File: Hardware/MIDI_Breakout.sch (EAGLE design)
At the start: 25 parts

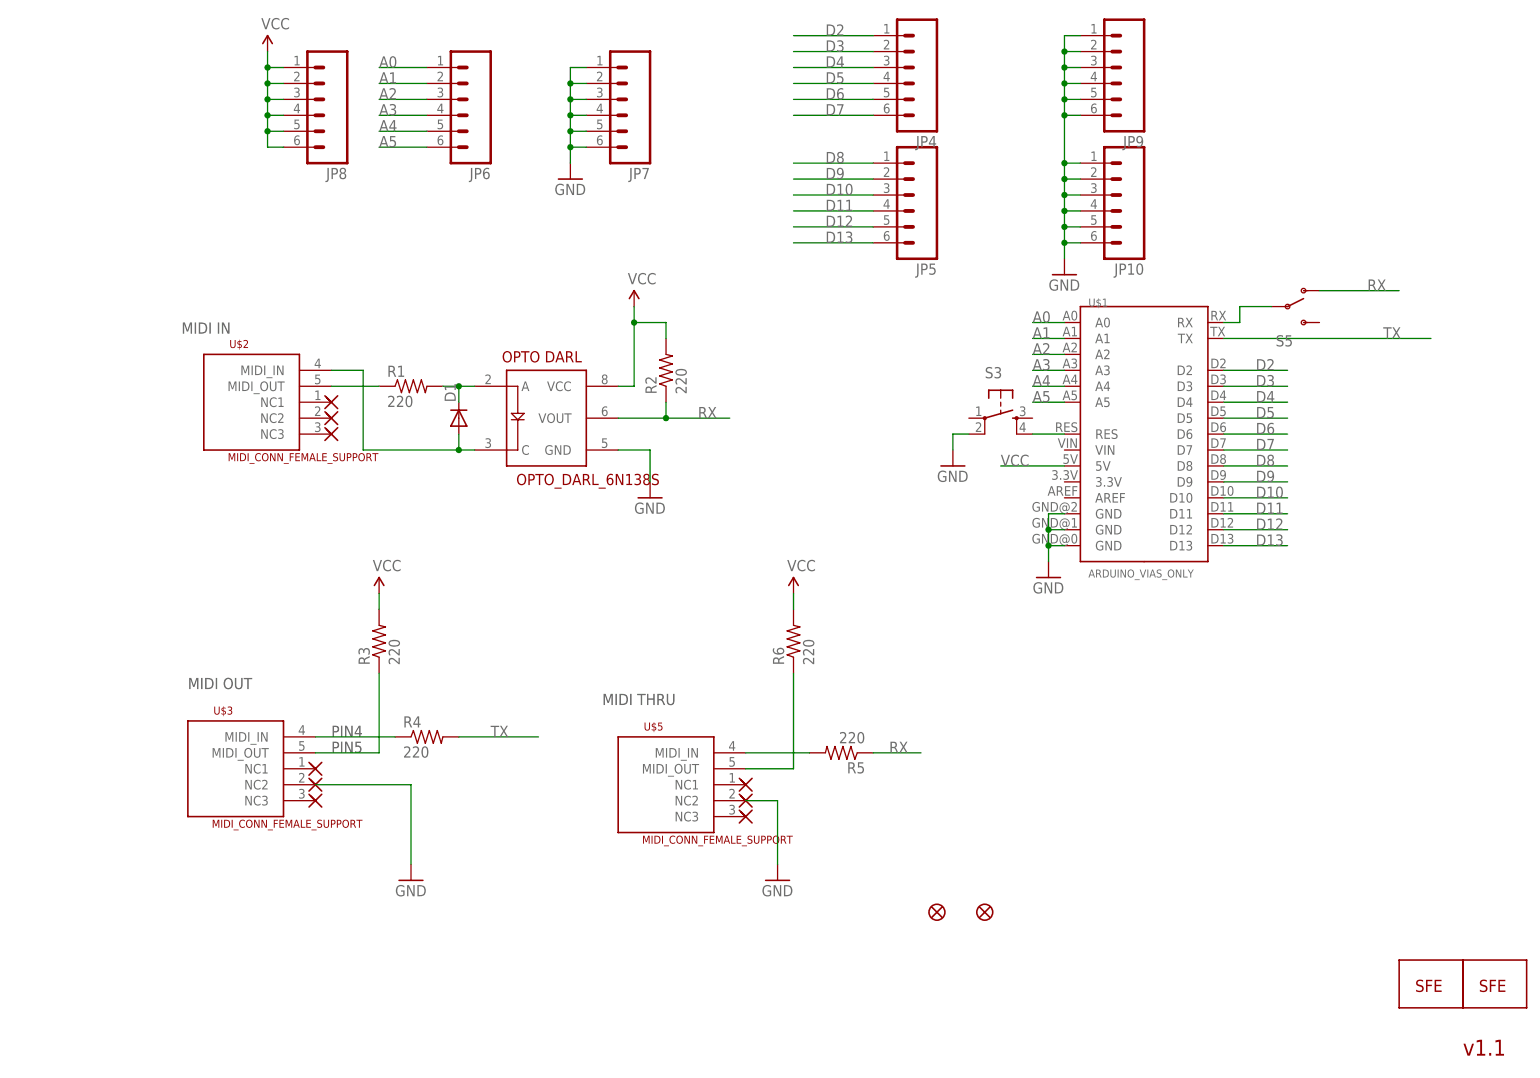
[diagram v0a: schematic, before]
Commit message: changed form factor, removed UNO pads, no more prog mode
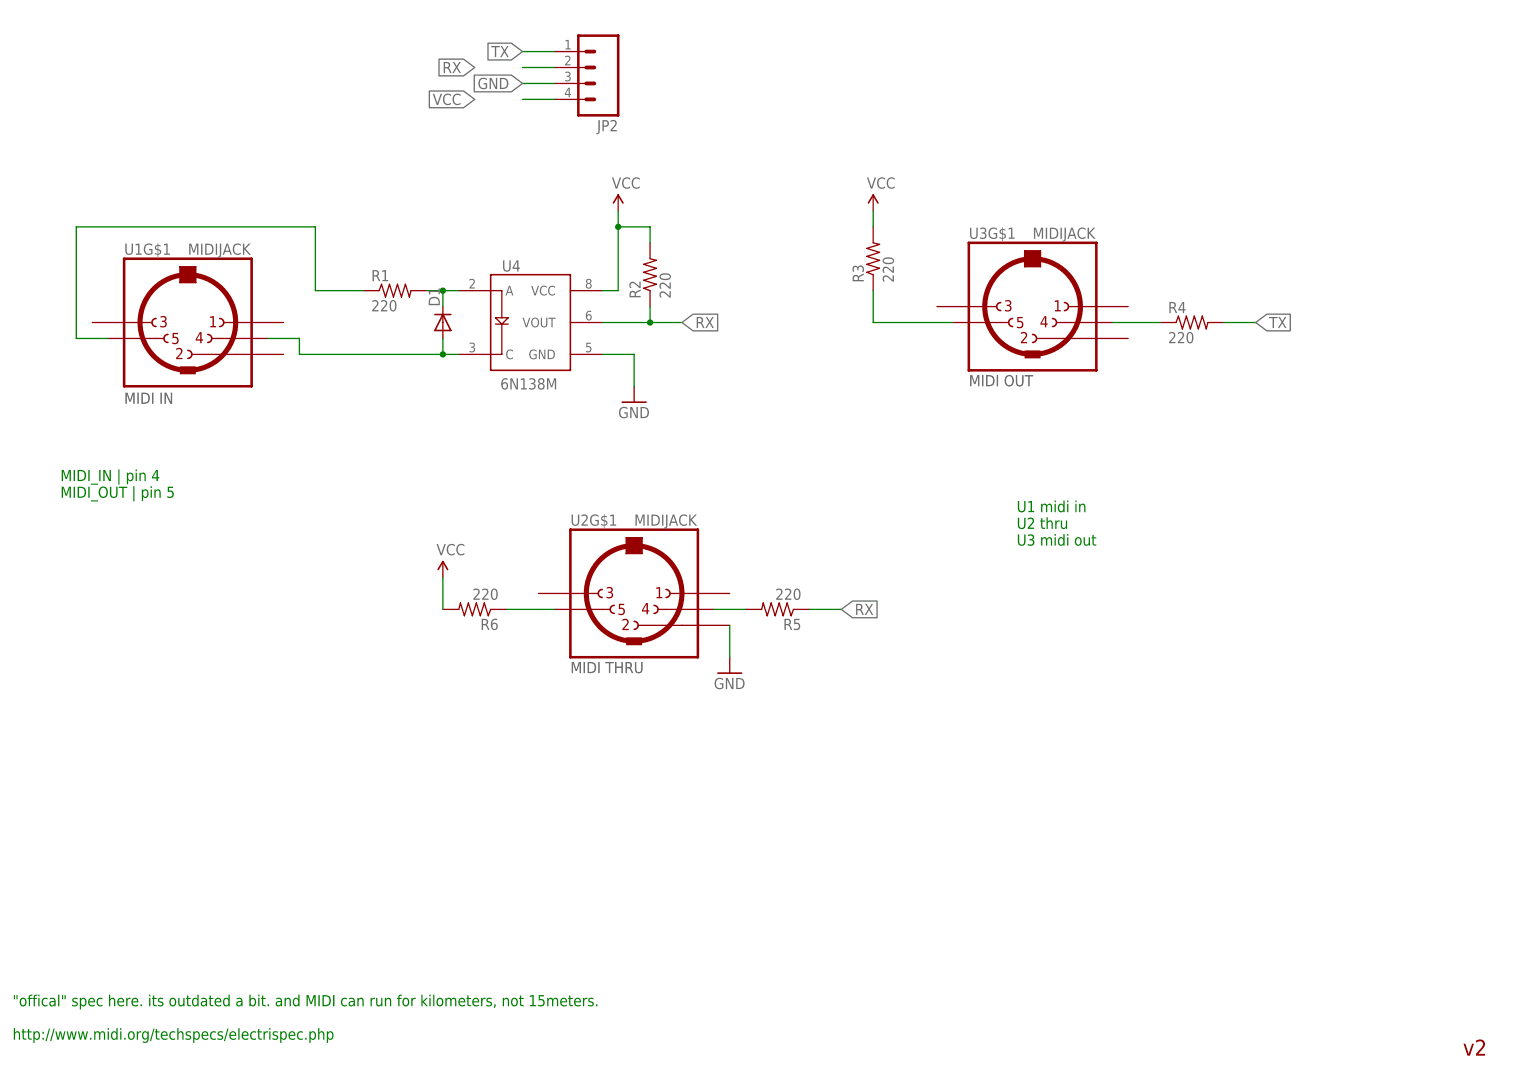
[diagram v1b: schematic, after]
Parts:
- removed JP1: FIDUCIAL1X2, SparkFun:FIDUCIAL1X2
- removed JP10, JP4, JP5, JP6, JP7, JP8, JP9: (no value), SparkFun:M06SIP
- removed JP11, JP3: LOGO-SFENEW, SparkFun:LOGO-SFENEW
- removed S3: (no value), SparkFun:TAC_SWITCHSMD
- removed S5: (no value), SparkFun:SWITCH-SPSTSMD
- removed U$1: ARDUINO_VIAS_ONLY, SparkFun:ARDUINO_VIAS_ONLY
- removed U$2, U$3, U$5: MIDI_CONN_FEMALE_SUPPORT, SparkFun:MIDI_CONN_FEMALE_SUPPORT
- removed U$6: OPTO_DARL_6N138S, SparkFun:OPTO_DARL_6N138S
- added U1, U2, U3: MIDIJACK, adafruit:MIDIJACK
- added U4: 6N138M, SparkFun-DiscreteSemi:OPTO_DARL_6N138S
- JP2: value FIDUCIAL1X2 -> (none); device SparkFun:FIDUCIAL1X2 -> SparkFun-Connectors:M041X04_NO_SILK
- R1, R2, R3, R4, R5, R6: device SparkFun:RESISTOR0402-RES -> adafruit:R-US_M0805
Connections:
- removed net A0: JP6.1, U$1.A0
- removed net A1: JP6.2, U$1.A1
- removed net A2: JP6.3, U$1.A2
- removed net A3: JP6.4, U$1.A3
- removed net A4: JP6.5, U$1.A4
- removed net A5: JP6.6, U$1.A5
- removed net D10: JP5.3, U$1.D10
- removed net D11: JP5.4, U$1.D11
- removed net D12: JP5.5, U$1.D12
- removed net D13: JP5.6, U$1.D13
- removed net D2: JP4.1, U$1.D2
- removed net D3: JP4.2, U$1.D3
- removed net D4: JP4.3, U$1.D4
- removed net D5: JP4.4, U$1.D5
- removed net D6: JP4.5, U$1.D6
- removed net D7: JP4.6, U$1.D7
- removed net D8: JP5.1, U$1.D8
- removed net D9: JP5.2, U$1.D9
- removed net N$4: S5.P, U$1.RX
- removed net N$5: S3.4, U$1.RES
- net 1235: now also U3G$1.5; no longer U$3.MIDI_OUT
- net 56: now also U4.A; no longer U$6.A
- net GND: now also JP2.3, U2G$1.2, U4.GND; no longer JP10.1, JP10.2, JP10.3, JP10.4, JP10.5, JP10.6, JP7.1, JP7.2, JP7.3, JP7.4, JP7.5, JP7.6, JP9.1, JP9.2, JP9.3, JP9.4, JP9.5, JP9.6, S3.2, U$1.GND@0, U$1.GND@1, U$1.GND@2, U$3.NC2, U$5.NC2, U$6.GND
- net N$1: now also U2G$1.5; no longer U$5.MIDI_OUT
- net N$2: now also U2G$1.4; no longer U$5.MIDI_IN
- net N$3: now also U1G$1.5; no longer U$2.MIDI_OUT
- net N$8: now also U3G$1.4; no longer U$3.MIDI_IN
- net PIN5: now also U1G$1.4, U4.C; no longer U$2.MIDI_IN, U$6.C
- net RX: now also JP2.2, U4.VOUT; no longer S5.O, U$6.VOUT
- net TX: now also JP2.1; no longer U$1.TX
- net VCC: now also JP2.4, U4.VCC; no longer JP8.1, JP8.2, JP8.3, JP8.4, JP8.5, JP8.6, U$1.5V, U$6.VCC
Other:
- note added: ""offical" spec here. its outdated a bit. and MIDI can run for kilometers, not 15meters. http://www.midi.org/techspecs/electrispec.php"
- note added: "MIDI_IN | pin 4 MIDI_OUT | pin 5"
- note added: "U1 midi in U2 thru U3 midi out"
- note added: "v2"
- note removed: "PIN4"
- note removed: "PIN5"
- note removed: "v1.1"
- moved on the sheet: D1, R1, R2, R3, R4, R5, R6

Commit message: mix thru hole and smd, layoutmostly
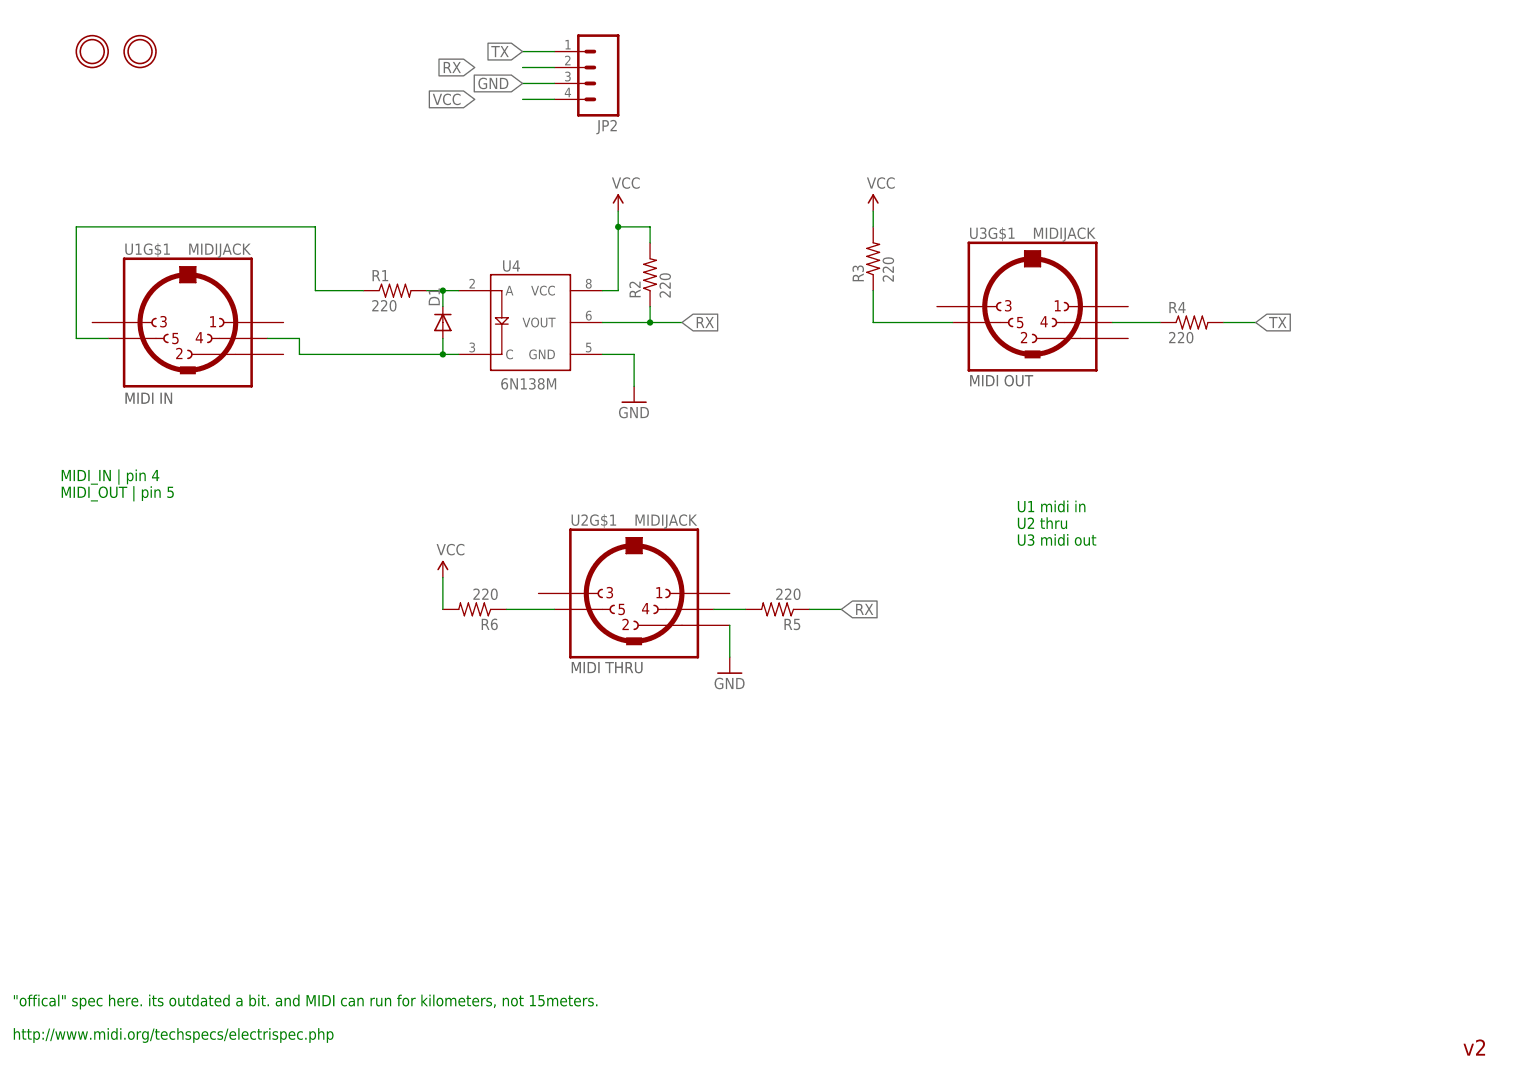
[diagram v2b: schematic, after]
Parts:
- added U$1, U$2: MOUNTINGHOLE, microbuilder:MOUNTINGHOLE
- R1, R2, R3, R4, R5, R6: device adafruit:R-US_M0805 -> SparkFun-Resistors:RESISTORPTH-1/2W
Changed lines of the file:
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@@
 <layer number="223" name="223bmp" color="24" fill="1" visible="no" active="no"/>
 <layer number="224" name="224bmp" color="25" fill="1" visible="no" active="no"/>
+<layer number="225" name="225bmp" color="7" fill="1" visible="yes" active="yes"/>
+<layer number="226" name="226bmp" color="7" fill="1" visible="yes" active="yes"/>
+<layer number="227" name="227bmp" color="7" fill="1" visible="yes" active="yes"/>
+<layer number="228" name="228bmp" color="7" fill="1" visible="yes" active="yes"/>
+<layer number="229" name="229bmp" color="7" fill="1" visible="yes" active="yes"/>
+<layer number="230" name="230bmp" color="7" fill="1" visible="yes" active="yes"/>
 <layer number="231" name="Eagle3D_PG1" color="7" fill="1" visible="no" active="no"/>
 <layer number="232" name="Eagle3D_PG2" color="7" fill="1" visible="no" active="no"/>
@@
 <part name="FRAME1" library="SparkFun" deviceset="FRAME-LETTER" device=""/>
 <part name="D1" library="SparkFun" deviceset="DIODE" device="SMA"/>
-<part name="R1" library="adafruit" deviceset="R-US_" device="M0805" value="220"/>
+<part name="R1" library="SparkFun-Resistors" deviceset="RESISTOR" device="PTH-1/2W" value="220"/>
 <part name="GND1" library="SparkFun" deviceset="GND" device=""/>
-<part name="R2" library="adafruit" deviceset="R-US_" device="M0805" value="220"/>
+<part name="R2" library="SparkFun-Resistors" deviceset="RESISTOR" device="PTH-1/2W" value="220"/>
 <part name="P+1" library="SparkFun" deviceset="VCC" device=""/>
-<part name="R3" library="adafruit" deviceset="R-US_" device="M0805" value="220"/>
-<part name="R4" library="adafruit" deviceset="R-US_" device="M0805" value="220"/>
+<part name="R3" library="SparkFun-Resistors" deviceset="RESISTOR" device="PTH-1/2W" value="220"/>
+<part name="R4" library="SparkFun-Resistors" deviceset="RESISTOR" device="PTH-1/2W" value="220"/>
 <part name="P+2" library="SparkFun" deviceset="VCC" device=""/>
 <part name="U4" library="SparkFun-DiscreteSemi" deviceset="OPTO_DARL_6N138S" device="" value="6N138M"/>
-<part name="R5" library="adafruit" deviceset="R-US_" device="M0805" value="220"/>
-<part name="R6" library="adafruit" deviceset="R-US_" device="M0805" value="220"/>
+<part name="R5" library="SparkFun-Resistors" deviceset="RESISTOR" device="PTH-1/2W" value="220"/>
+<part name="R6" library="SparkFun-Resistors" deviceset="RESISTOR" device="PTH-1/2W" value="220"/>
 <part name="P+4" library="SparkFun" deviceset="VCC" device=""/>
 <part name="GND7" library="SparkFun" deviceset="GND" device=""/>
@@
 <part name="U2" library="adafruit" deviceset="MIDIJACK" device=""/>
 <part name="JP2" library="SparkFun-Connectors" deviceset="M04" device="1X04_NO_SILK"/>
+<part name="U$1" library="microbuilder" deviceset="MOUNTINGHOLE" device=""/>
+<part name="U$2" library="microbuilder" deviceset="MOUNTINGHOLE" device=""/>
 </parts>
 <sheets>
@@
 <instance part="U2" gate="G$1" x="106.68" y="81.28"/>
 <instance part="JP2" gate="G$1" x="99.06" y="165.1" rot="R180"/>
+<instance part="U$1" gate="G$1" x="20.32" y="167.64"/>
+<instance part="U$2" gate="G$1" x="27.94" y="167.64"/>
 </instances>
 <busses>
